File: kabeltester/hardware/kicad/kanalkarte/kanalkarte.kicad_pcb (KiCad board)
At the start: 4 copper layers, 118 x 74 mm, 413 parts, among them J1 DIN 41612 C96 Feder, J2 Messkarte, U1 SN74HC595PW, U10 CD74HCT4067M96, U11 ADG1606BRUZ, U12 CD74HCT4067M96, U13 ADG1606BRUZ, U14 CD74HCT4067M96, U15 ADG1606BRUZ, U16 CD74HCT4067M96, U17 ADG1606BRUZ, U18 CD74HCT4067M96, U2 SN74HC595PW, U3 ADG1606BRUZ, U4 CD74HCT4067M96, U5 ADG1606BRUZ, U6 CD74HCT4067M96, U7 ADG1606BRUZ, U8 CD74HCT4067M96, U9 ADG1606BRUZ

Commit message: Kanalkarte: Routing-Endstand (945 -> 292 offen), Masse-Vias, DRC und Fertigungsdaten
Freerouting hängt in Runde 3; mit 4 Lagen kein weiterer Fortschritt.

Co-Authored-By: Claude Opus 5.5 <noreply@anthropic.com>
Claude-Session: https://claude.ai/code/session_0119zGeGQCWTR3UwpEi96iWe
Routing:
- net GND: track 0.00 -> 23.2 mm, vias 0 -> 73
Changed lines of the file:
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@@
   (segment (start 98.0999 4.28) (end 98.0999 3.1536) (width 0.2) (layer "B.Cu") (net 148))
   (segment (start 96.6862 2.5938) (end 95.5099 1.4175) (width 0.2) (layer "B.Cu") (net 148))
+  (segment (start 90.4 14) (end 90.4 15.975) (width 0.25) (layer "F.Cu") (net 149))
+  (segment (start 25.5125 9.524999) (end 23.025 9.524999) (width 0.25) (layer "F.Cu") (net 149))
+  (segment (start 90.4 14) (end 90.4 15.975) (width 0.25) (layer "F.Cu") (net 149))
+  (segment (start 42.079969 56.157498) (end 42.079969 54.919998) (width 0.25) (layer "F.Cu") (net 149))
+  (via (at 69.978093 59.198) (size 0.6) (drill 0.3) (layers "F.Cu" "B.Cu") (net 149))
+  (via (at 78.7 16.2) (size 0.6) (drill 0.3) (layers "F.Cu" "B.Cu") (net 149))
+  (via (at 23.971227 18.528399) (size 0.6) (drill 0.3) (layers "F.Cu" "B.Cu") (net 149))
+  (via (at 8.7105 58.821564) (size 0.6) (drill 0.3) (layers "F.Cu" "B.Cu") (net 149))
+  (via (at 99.277798 15.116984) (size 0.6) (drill 0.3) (layers "F.Cu" "B.Cu") (net 149))
+  (via (at 106.2 71.2) (size 0.6) (drill 0.3) (layers "F.Cu" "B.Cu") (net 149))
+  (via (at 58.0505 16.8151) (size 0.6) (drill 0.3) (layers "F.Cu" "B.Cu") (net 149))
+  (via (at 60.9005 31.882249) (size 0.6) (drill 0.3) (layers "F.Cu" "B.Cu") (net 149))
+  (via (at 16.2 31.2) (size 0.6) (drill 0.3) (layers "F.Cu" "B.Cu") (net 149))
+  (via (at 34.911467 4.7961) (size 0.6) (drill 0.3) (layers "F.Cu" "B.Cu") (net 149))
+  (via (at 56.2 31.2) (size 0.6) (drill 0.3) (layers "F.Cu" "B.Cu") (net 149))
+  (via (at 24.311418 66.5955) (size 0.6) (drill 0.3) (layers "F.Cu" "B.Cu") (net 149))
+  (via (at 21.806686 61.655768) (size 0.6) (drill 0.3) (layers "F.Cu" "B.Cu") (net 149))
+  (via (at 35.789485 59.698) (size 0.6) (drill 0.3) (layers "F.Cu" "B.Cu") (net 149))
+  (via (at 6.2 31.2) (size 0.6) (drill 0.3) (layers "F.Cu" "B.Cu") (net 149))
+  (via (at 51.2 41.2) (size 0.6) (drill 0.3) (layers "F.Cu" "B.Cu") (net 149))
+  (via (at 34.719417 7.91304) (size 0.6) (drill 0.3) (layers "F.Cu" "B.Cu") (net 149))
+  (via (at 96.2 71.2) (size 0.6) (drill 0.3) (layers "F.Cu" "B.Cu") (net 149))
+  (via (at 27.997664 7.4255) (size 0.6) (drill 0.3) (layers "F.Cu" "B.Cu") (net 149))
+  (via (at 13.7 56.2) (size 0.6) (drill 0.3) (layers "F.Cu" "B.Cu") (net 149))
+  (via (at 106.2 61.2) (size 0.6) (drill 0.3) (layers "F.Cu" "B.Cu") (net 149))
+  (via (at 23.8605 35.1774) (size 0.6) (drill 0.3) (layers "F.Cu" "B.Cu") (net 149))
+  (via (at 101.2 71.2) (size 0.6) (drill 0.3) (layers "F.Cu" "B.Cu") (net 149))
+  (via (at 54.337462 13.4314) (size 0.6) (drill 0.3) (layers "F.Cu" "B.Cu") (net 149))
+  (via (at 64.387462 2.6358) (size 0.6) (drill 0.3) (layers "F.Cu" "B.Cu") (net 149))
+  (via (at 42.079969 54.919998) (size 0.6) (drill 0.3) (layers "F.Cu" "B.Cu") (net 149))
+  (via (at 59.8305 39.952107) (size 0.6) (drill 0.3) (layers "F.Cu" "B.Cu") (net 149))
+  (via (at 91.2 21.2) (size 0.6) (drill 0.3) (layers "F.Cu" "B.Cu") (net 149))
+  (via (at 96.2 21.2) (size 0.6) (drill 0.3) (layers "F.Cu" "B.Cu") (net 149))
+  (via (at 77.580929 7.833986) (size 0.6) (drill 0.3) (layers "F.Cu" "B.Cu") (net 149))
+  (via (at 82.863196 1.4423) (size 0.6) (drill 0.3) (layers "F.Cu" "B.Cu") (net 149))
+  (via (at 24.910487 43.184926) (size 0.6) (drill 0.3) (layers "F.Cu" "B.Cu") (net 149))
+  (via (at 15.0756 2.8675) (size 0.6) (drill 0.3) (layers "F.Cu" "B.Cu") (net 149))
+  (via (at 110.681177 19.259199) (size 0.6) (drill 0.3) (layers "F.Cu" "B.Cu") (net 149))
+  (via (at 8.7 56.2) (size 0.6) (drill 0.3) (layers "F.Cu" "B.Cu") (net 149))
+  (via (at 25.331598 50.051497) (size 0.6) (drill 0.3) (layers "F.Cu" "B.Cu") (net 149))
+  (via (at 68.037512 16.3055) (size 0.6) (drill 0.3) (layers "F.Cu" "B.Cu") (net 149))
+  (via (at 8.6925 2.6175) (size 0.6) (drill 0.3) (layers "F.Cu" "B.Cu") (net 149))
+  (via (at 11.2 31.2) (size 0.6) (drill 0.3) (layers "F.Cu" "B.Cu") (net 149))
+  (via (at 1.2 11.2) (size 0.6) (drill 0.3) (layers "F.Cu" "B.Cu") (net 149))
+  (via (at 13.688879 64.4316) (size 0.6) (drill 0.3) (layers "F.Cu" "B.Cu") (net 149))
+  (via (at 59.868717 1.952779) (size 0.6) (drill 0.3) (layers "F.Cu" "B.Cu") (net 149))
+  (via (at 3.7 26.2) (size 0.6) (drill 0.3) (layers "F.Cu" "B.Cu") (net 149))
+  (via (at 53.7 56.2) (size 0.6) (drill 0.3) (layers "F.Cu" "B.Cu") (net 149))
+  (via (at 23.025 9.524999) (size 0.6) (drill 0.3) (layers "F.Cu" "B.Cu") (net 149))
+  (via (at 11.9755 18.443837) (size 0.6) (drill 0.3) (layers "F.Cu" "B.Cu") (net 149))
+  (via (at 113.7 66.2) (size 0.6) (drill 0.3) (layers "F.Cu" "B.Cu") (net 149))
+  (via (at 73.259953 38.479996) (size 0.6) (drill 0.3) (layers "F.Cu" "B.Cu") (net 149))
+  (via (at 8.7 46.2) (size 0.6) (drill 0.3) (layers "F.Cu" "B.Cu") (net 149))
+  (via (at 109.946697 46.5685) (size 0.6) (drill 0.3) (layers "F.Cu" "B.Cu") (net 149))
+  (via (at 20.3328 59.850573) (size 0.6) (drill 0.3) (layers "F.Cu" "B.Cu") (net 149))
+  (via (at 93.758009 2.1923) (size 0.6) (drill 0.3) (layers "F.Cu" "B.Cu") (net 149))
+  (via (at 90.4 15.975) (size 0.6) (drill 0.3) (layers "F.Cu" "B.Cu") (net 149))
+  (via (at 47.905574 12.3695) (size 0.6) (drill 0.3) (layers "F.Cu" "B.Cu") (net 149))
+  (via (at 24.082498 2.65) (size 0.6) (drill 0.3) (layers "F.Cu" "B.Cu") (net 149))
+  (via (at 30.326461 39.175133) (size 0.6) (drill 0.3) (layers "F.Cu" "B.Cu") (net 149))
+  (via (at 46.445513 16.528399) (size 0.6) (drill 0.3) (layers "F.Cu" "B.Cu") (net 149))
+  (via (at 71.604484 30.4393) (size 0.6) (drill 0.3) (layers "F.Cu" "B.Cu") (net 149))
+  (via (at 5.7401 48.0805) (size 0.6) (drill 0.3) (layers "F.Cu" "B.Cu") (net 149))
+  (via (at 29.7005 65.638) (size 0.6) (drill 0.3) (layers "F.Cu" "B.Cu") (net 149))
+  (via (at 80.9904 50.1402) (size 0.6) (drill 0.3) (layers "F.Cu" "B.Cu") (net 149))
+  (via (at 51.2 61.2) (size 0.6) (drill 0.3) (layers "F.Cu" "B.Cu") (net 149))
+  (via (at 106.2 51.2) (size 0.6) (drill 0.3) (layers "F.Cu" "B.Cu") (net 149))
+  (via (at 3.7 66.2) (size 0.6) (drill 0.3) (layers "F.Cu" "B.Cu") (net 149))
+  (via (at 21.115559 7.9405) (size 0.6) (drill 0.3) (layers "F.Cu" "B.Cu") (net 149))
+  (via (at 20.041489 39.5881) (size 0.6) (drill 0.3) (layers "F.Cu" "B.Cu") (net 149))
+  (via (at 65.901723 7.937898) (size 0.6) (drill 0.3) (layers "F.Cu" "B.Cu") (net 149))
+  (via (at 55.000465 18.4363) (size 0.6) (drill 0.3) (layers "F.Cu" "B.Cu") (net 149))
+  (via (at 37.07751 69.2019) (size 0.6) (drill 0.3) (layers "F.Cu" "B.Cu") (net 149))
+  (via (at 109.602728 0.9) (size 0.6) (drill 0.3) (layers "F.Cu" "B.Cu") (net 149))
+  (via (at 89.06243 6.255014) (size 0.6) (drill 0.3) (layers "F.Cu" "B.Cu") (net 149))
+  (via (at 32.726304 13.9752) (size 0.6) (drill 0.3) (layers "F.Cu" "B.Cu") (net 149))
+  (via (at 3.2672 15.1165) (size 0.6) (drill 0.3) (layers "F.Cu" "B.Cu") (net 149))
+  (segment (start 58.999967 3.457499) (end 59.868717 1.952779) (width 0.25) (layer "B.Cu") (net 149))
+  (segment (start 67.129956 11.402495) (end 65.901723 7.937898) (width 0.25) (layer "B.Cu") (net 149))
+  (segment (start 73.259953 40.467496) (end 73.259953 38.479996) (width 0.25) (layer "B.Cu") (net 149))
+  (segment (start 86.949949 8.367495) (end 89.06243 6.255014) (width 0.25) (layer "B.Cu") (net 149))
+  (segment (start 34.799983 8.367495) (end 34.719417 7.91304) (width 0.25) (layer "B.Cu") (net 149))
+  (segment (start 34.799983 8.367495) (end 34.719417 7.91304) (width 0.25) (layer "B.Cu") (net 149))
+  (segment (start 86.949949 8.367495) (end 89.06243 6.255014) (width 0.25) (layer "B.Cu") (net 149))
+  (segment (start 111.299928 18.187493) (end 110.681177 19.259199) (width 0.25) (layer "B.Cu") (net 149))
   (segment (start 20.0563 48.0147) (end 7.6312 48.0147) (width 0.2) (layer "F.Cu") (net 150))
   (segment (start 64.2587 10.7666) (end 65.5003 9.525) (width 0.2) (layer "F.Cu") (net 150))

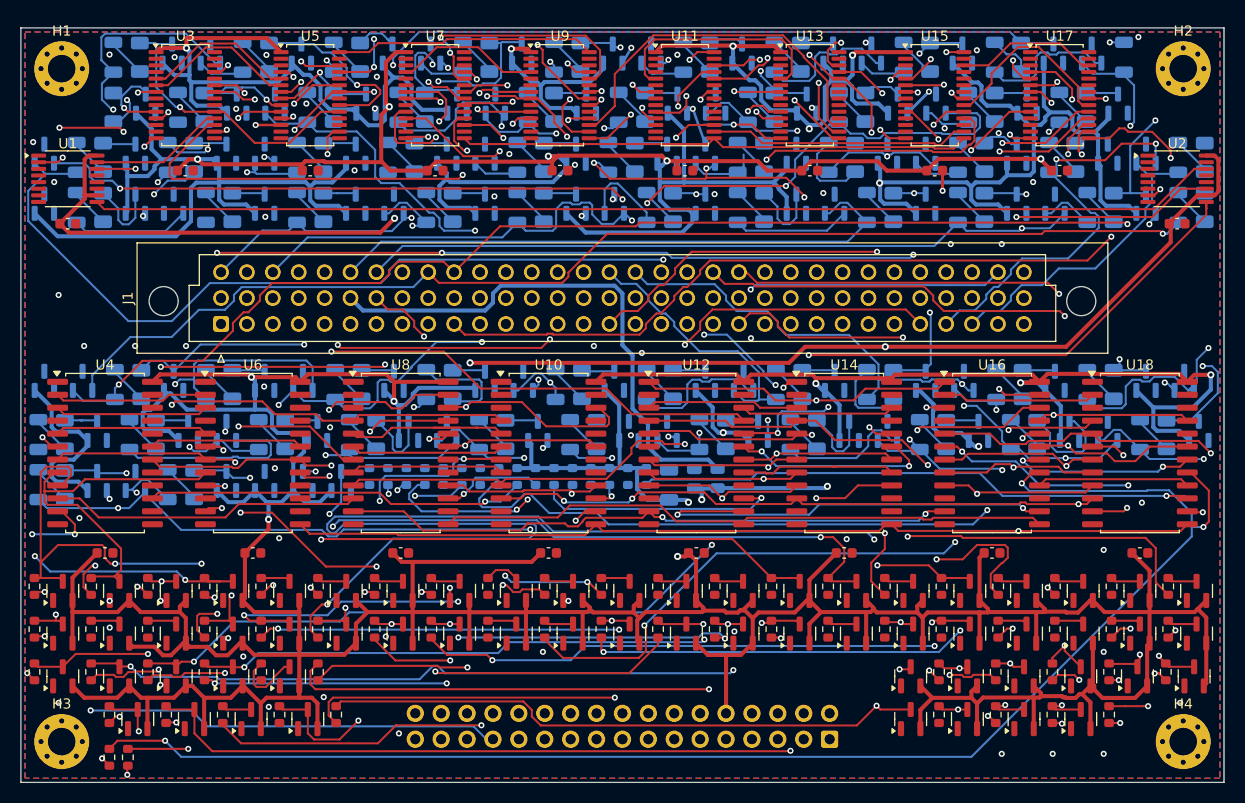
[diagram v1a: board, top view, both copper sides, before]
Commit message: Kanalkarte auf 6 Lagen (In1 GND, In2-In4 + Außenlagen Signal), ungeroutet
Generator: Lagentypen und Gerber-Lagenliste für beliebige Lagenzahl.

Co-Authored-By: Claude Opus 5.5 <noreply@anthropic.com>
Claude-Session: https://claude.ai/code/session_0119zGeGQCWTR3UwpEi96iWe
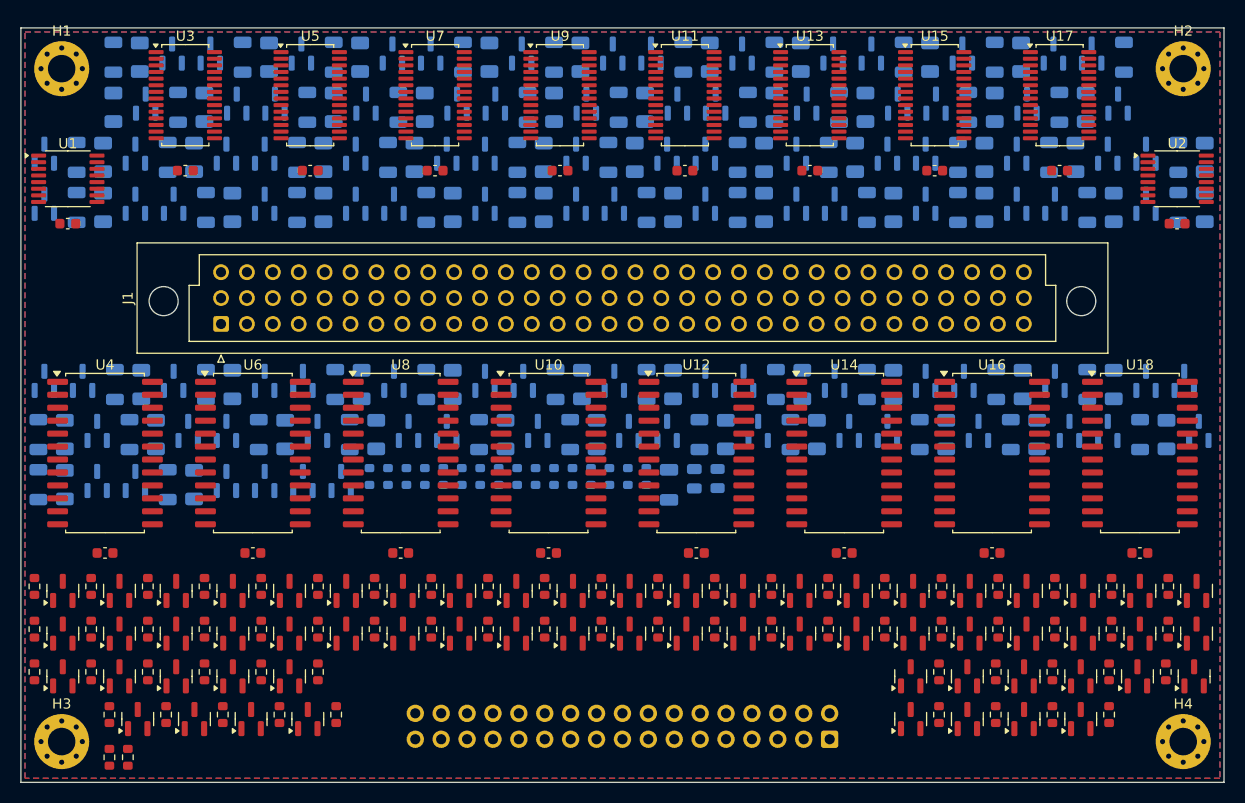
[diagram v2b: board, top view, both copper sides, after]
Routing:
- net 5VA: track 1130.4 -> 0.00 mm, vias 21 -> 0
- net 3V3: track 202.3 -> 0.00 mm, vias 5 -> 0
- net HA3: track 191.9 -> 0.00 mm, vias 6 -> 0
- net S63: track 180.2 -> 0.00 mm, vias 4 -> 0
- net HA1: track 172.3 -> 0.00 mm, vias 7 -> 0
- net TP42: track 165.7 -> 0.00 mm, vias 3 -> 0
- net TP64: track 163.8 -> 0.00 mm, vias 2 -> 0
- net LA0: track 161.8 -> 0.00 mm, vias 4 -> 0
- net TP41: track 160.1 -> 0.00 mm, vias 2 -> 0
- net LA1: track 159.2 -> 0.00 mm, vias 6 -> 0
- net TP27: track 157.4 -> 0.00 mm, vias 3 -> 0
- net LA3: track 140.6 -> 0.00 mm, vias 3 -> 0
- net TP63: track 137.2 -> 0.00 mm, vias 4 -> 0
- net F63: track 128.1 -> 0.00 mm, vias 3 -> 0
- net S54: track 125.3 -> 0.00 mm, vias 2 -> 0
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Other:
- copper layers 4 -> 6
